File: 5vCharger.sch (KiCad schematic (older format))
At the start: 12 parts

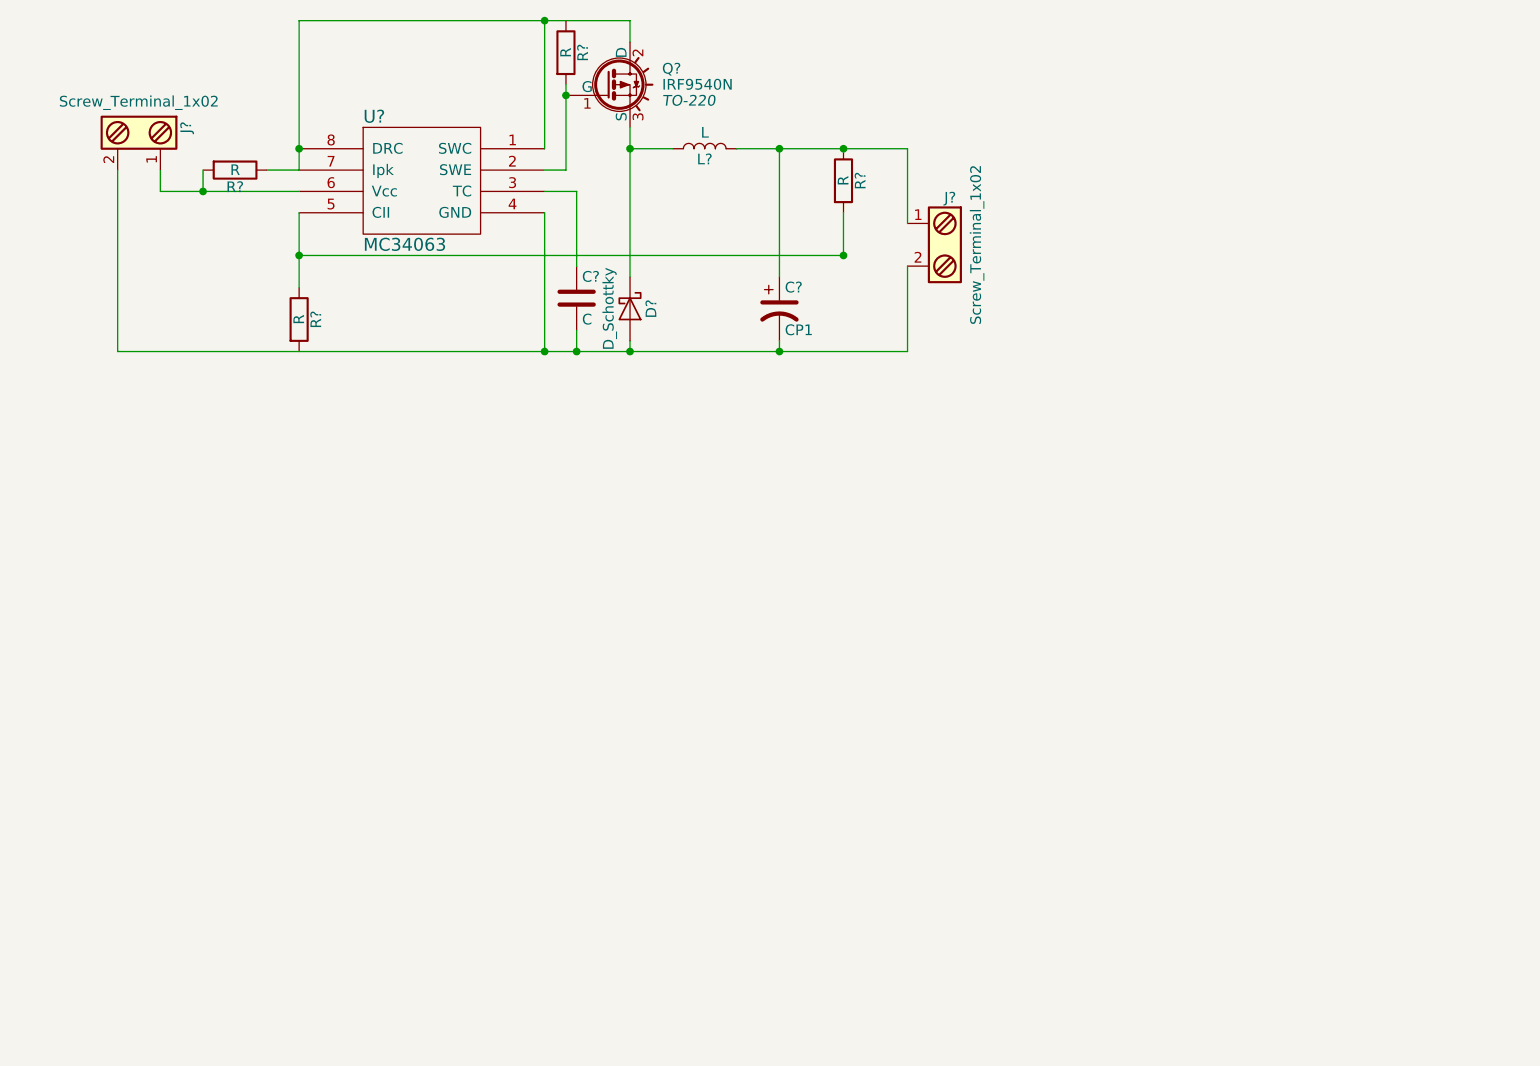
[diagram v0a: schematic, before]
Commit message: Set component values
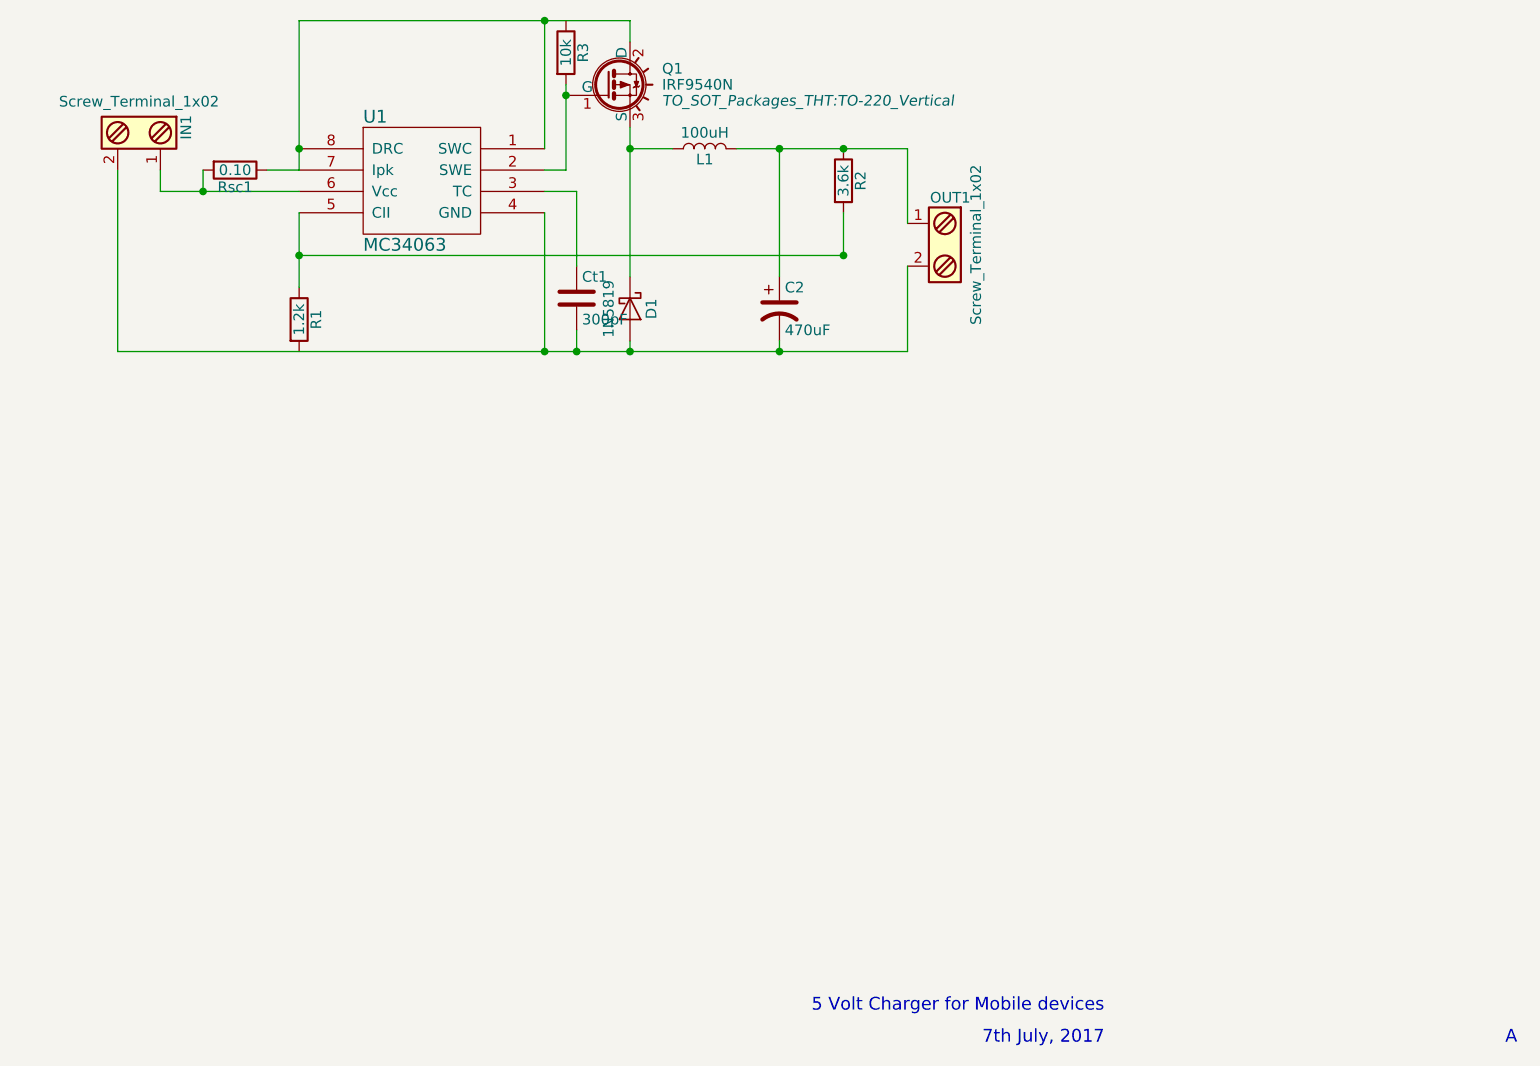
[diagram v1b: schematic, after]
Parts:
- C2: renamed from C?; value CP1 -> 470uF
- Ct1: renamed from C?; value C -> 300pF; footprint (none) -> Capacitors_THT:C_Disc_D4.3mm_W1.9mm_P5.00mm
- D1: renamed from D?; value D_Schottky -> 1N5819; footprint (none) -> Diodes_THT:D_DO-41_SOD81_P10.16mm_Horizontal
- IN1, OUT1: renamed from J?; footprint (none) -> Connectors_Terminal_Blocks:TerminalBlock_Pheonix_MKDS1.5-2pol
- L1: renamed from L?; value L -> 100uH
- Q1: renamed from Q?; footprint TO-220 -> TO_SOT_Packages_THT:TO-220_Vertical
- R1: renamed from R?; value R -> 1.2k
- R2: renamed from R?; value R -> 3.6k
- R3: renamed from R?; value R -> 10k
- Rsc1: renamed from R?; value R -> 0.10
- gave numbers to parts that had none: 1
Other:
- note added: "5 Volt Charger for Mobile devices"
- note added: "7th July, 2017"
- note added: "A"
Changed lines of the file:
@@
 LIBS:valves
 LIBS:MC34063
+LIBS:5vCharger-cache
 EELAYER 25 0
 EELAYER END
@@
 $EndDescr
 $Comp
-L MC34063 U?
+L MC34063 U1
 U 1 1 59883D9D
 P 5550 3650
-F 0 "U?" H 5250 4000 60  0000 L CNN
+F 0 "U1" H 5250 4000 60  0000 L CNN
 F 1 "MC34063" H 5250 3400 60  0000 L CNN
-F 2 "" H 5450 3650 60  0000 C CNN
+F 2 "" H 5450 3650 60  0001 C CNN
 F 3 "" H 5450 3650 60  0000 C CNN
 	1    5550 3650
@@
 Connection ~ 4950 3450
 $Comp
-L R R?
+L R Rsc1
 U 1 1 59883E1F
 P 4650 3550
-F 0 "R?" V 4730 3550 50  0000 C CNN
-F 1 "R" V 4650 3550 50  0000 C CNN
-F 2 "" V 4580 3550 50  0000 C CNN
+F 0 "Rsc1" V 4730 3550 50  0000 C CNN
+F 1 "0.10" V 4650 3550 50  0000 C CNN
+F 2 "" V 4580 3550 50  0001 C CNN
 F 3 "" H 4650 3550 50  0000 C CNN
 	1    4650 3550
@@
 Connection ~ 4500 3650
 $Comp
-L Screw_Terminal_1x02 J?
+L Screw_Terminal_1x02 IN1
 U 1 1 59883FF8
 P 4200 3350
-F 0 "J?" H 4200 3600 50  0000 C TNN
+F 0 "IN1" H 4200 3600 50  0000 C TNN
 F 1 "Screw_Terminal_1x02" V 4050 3350 50  0000 C TNN
-F 2 "" H 4200 3125 50  0001 C CNN
+F 2 "Connectors_Terminal_Blocks:TerminalBlock_Pheonix_MKDS1.5-2pol" H 4200 3125 50  0001 C CNN
 F 3 "" H 4175 3350 50  0001 C CNN
 	1    4200 3350
@@
 	4100 4400 7800 4400
 $Comp
-L IRF9540N Q?
+L IRF9540N Q1
 U 1 1 5988468A
 P 6400 3150
-F 0 "Q?" H 6650 3225 50  0000 L CNN
+F 0 "Q1" H 6650 3225 50  0000 L CNN
 F 1 "IRF9540N" H 6650 3150 50  0000 L CNN
-F 2 "TO-220" H 6650 3075 50  0000 L CIN
+F 2 "TO_SOT_Packages_THT:TO-220_Vertical" H 6650 3075 50  0000 L CIN
 F 3 "" H 6400 3150 50  0000 L CNN
 	1    6400 3150
@@
 $EndComp
 $Comp
-L R R?
+L R R3
 U 1 1 59884753
 P 6200 3000
-F 0 "R?" V 6280 3000 50  0000 C CNN
-F 1 "R" V 6200 3000 50  0000 C CNN
-F 2 "" V 6130 3000 50  0000 C CNN
+F 0 "R3" V 6280 3000 50  0000 C CNN
+F 1 "10k" V 6200 3000 50  0000 C CNN
+F 2 "" V 6130 3000 50  0001 C CNN
 F 3 "" H 6200 3000 50  0000 C CNN
 	1    6200 3000
@@
 	6500 2850 6500 2950
 $Comp
-L D_Schottky D?
+L D_Schottky D1
 U 1 1 598847EF
 P 6500 4200
-F 0 "D?" H 6500 4300 50  0000 C CNN
-F 1 "D_Schottky" H 6500 4100 50  0000 C CNN
-F 2 "" H 6500 4200 50  0000 C CNN
+F 0 "D1" H 6500 4300 50  0000 C CNN
+F 1 "1N5819" H 6500 4100 50  0000 C CNN
+F 2 "Diodes_THT:D_DO-41_SOD81_P10.16mm_Horizontal" H 6500 4200 50  0001 C CNN
 F 3 "" H 6500 4200 50  0000 C CNN
 	1    6500 4200
@@
 	6500 3350 6500 4050
 $Comp
-L L L?
+L L L1
 U 1 1 59884843
 P 6850 3450
-F 0 "L?" V 6800 3450 50  0000 C CNN
-F 1 "L" V 6925 3450 50  0000 C CNN
-F 2 "" H 6850 3450 50  0000 C CNN
+F 0 "L1" V 6800 3450 50  0000 C CNN
+F 1 "100uH" V 6925 3450 50  0000 C CNN
+F 2 "" H 6850 3450 50  0001 C CNN
 F 3 "" H 6850 3450 50  0000 C CNN
 	1    6850 3450
@@
 $EndComp
 $Comp
-L CP1 C?
+L CP1 C2
 U 1 1 59884893
 P 7200 4200
-F 0 "C?" H 7225 4300 50  0000 L CNN
-F 1 "CP1" H 7225 4100 50  0000 L CNN
-F 2 "" H 7200 4200 50  0000 C CNN
+F 0 "C2" H 7225 4300 50  0000 L CNN
+F 1 "470uF" H 7225 4100 50  0000 L CNN
+F 2 "" H 7200 4200 50  0001 C CNN
 F 3 "" H 7200 4200 50  0000 C CNN
 	1    7200 4200
@@
 Connection ~ 7200 3450
 $Comp
-L R R?
+L R R2
 U 1 1 5988498A
 P 7500 3600
-F 0 "R?" V 7580 3600 50  0000 C CNN
-F 1 "R" V 7500 3600 50  0000 C CNN
-F 2 "" V 7430 3600 50  0000 C CNN
+F 0 "R2" V 7580 3600 50  0000 C CNN
+F 1 "3.6k" V 7500 3600 50  0000 C CNN
+F 2 "" V 7430 3600 50  0001 C CNN
 F 3 "" H 7500 3600 50  0000 C CNN
 	1    7500 3600
@@
 Connection ~ 6200 3200
 $Comp
-L R R?
+L R R1
 U 1 1 59884CE2
 P 4950 4250
-F 0 "R?" V 5030 4250 50  0000 C CNN
-F 1 "R" V 4950 4250 50  0000 C CNN
-F 2 "" V 4880 4250 50  0000 C CNN
+F 0 "R1" V 5030 4250 50  0000 C CNN
+F 1 "1.2k" V 4950 4250 50  0000 C CNN
+F 2 "" V 4880 4250 50  0001 C CNN
 F 3 "" H 4950 4250 50  0000 C CNN
 	1    4950 4250
@@
 	7500 3950 7500 3750
 $Comp
-L C C?
+L C Ct1
 U 1 1 59884EE9
 P 6250 4150
-F 0 "C?" H 6275 4250 50  0000 L CNN
-F 1 "C" H 6275 4050 50  0000 L CNN
-F 2 "" H 6288 4000 50  0000 C CNN
+F 0 "Ct1" H 6275 4250 50  0000 L CNN
+F 1 "300pF" H 6275 4050 50  0000 L CNN
+F 2 "Capacitors_THT:C_Disc_D4.3mm_W1.9mm_P5.00mm" H 6288 4000 50  0001 C CNN
 F 3 "" H 6250 4150 50  0000 C CNN
 	1    6250 4150
@@
 Connection ~ 4950 3950
 $Comp
-L Screw_Terminal_1x02 J?
+L Screw_Terminal_1x02 OUT1
 U 1 1 59885326
 P 8000 3900
-F 0 "J?" H 8000 4150 50  0000 C TNN
+F 0 "OUT1" H 8000 4150 50  0000 C TNN
 F 1 "Screw_Terminal_1x02" V 7850 3900 50  0000 C TNN
-F 2 "" H 8000 3675 50  0001 C CNN
+F 2 "Connectors_Terminal_Blocks:TerminalBlock_Pheonix_MKDS1.5-2pol" H 8000 3675 50  0001 C CNN
 F 3 "" H 7975 3900 50  0001 C CNN
 	1    8000 3900
@@
 	6100 3450 6100 2850
 Connection ~ 6100 2850
+Text Notes 7350 7500 0    60   ~ 0
+5 Volt Charger for Mobile devices
+Text Notes 10600 7650 0    60   ~ 0
+A
+Text Notes 8150 7650 0    60   ~ 0
+7th July, 2017
 $EndSCHEMATC

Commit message: Generated netlist
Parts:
- C2: footprint (none) -> Capacitors_THT:CP_Radial_D14.0mm_P5.00mm
- L1: footprint (none) -> Choke_Toroid_ThroughHole:Choke_Toroid_5x10mm_Vertical
- R1, R2, R3: footprint (none) -> Resistors_THT:R_Axial_DIN0207_L6.3mm_D2.5mm_P10.16mm_Horizontal
- Rsc1: footprint (none) -> Resistors_THT:R_Axial_DIN0918_L18.0mm_D9.0mm_P7.62mm_Vertical
- U1: footprint (none) -> Housings_DIP:DIP-8_W7.62mm_LongPads
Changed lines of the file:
@@
 F 0 "U1" H 5250 4000 60  0000 L CNN
 F 1 "MC34063" H 5250 3400 60  0000 L CNN
-F 2 "" H 5450 3650 60  0001 C CNN
+F 2 "Housings_DIP:DIP-8_W7.62mm_LongPads" H 5450 3650 60  0001 C CNN
 F 3 "" H 5450 3650 60  0000 C CNN
 	1    5550 3650
@@
 F 0 "Rsc1" V 4730 3550 50  0000 C CNN
 F 1 "0.10" V 4650 3550 50  0000 C CNN
-F 2 "" V 4580 3550 50  0001 C CNN
+F 2 "Resistors_THT:R_Axial_DIN0918_L18.0mm_D9.0mm_P7.62mm_Vertical" V 4580 3550 50  0001 C CNN
 F 3 "" H 4650 3550 50  0000 C CNN
 	1    4650 3550
@@
 F 0 "R3" V 6280 3000 50  0000 C CNN
 F 1 "10k" V 6200 3000 50  0000 C CNN
-F 2 "" V 6130 3000 50  0001 C CNN
+F 2 "Resistors_THT:R_Axial_DIN0207_L6.3mm_D2.5mm_P10.16mm_Horizontal" V 6130 3000 50  0001 C CNN
 F 3 "" H 6200 3000 50  0000 C CNN
 	1    6200 3000
@@
 F 0 "L1" V 6800 3450 50  0000 C CNN
 F 1 "100uH" V 6925 3450 50  0000 C CNN
-F 2 "" H 6850 3450 50  0001 C CNN
+F 2 "Choke_Toroid_ThroughHole:Choke_Toroid_5x10mm_Vertical" H 6850 3450 50  0001 C CNN
 F 3 "" H 6850 3450 50  0000 C CNN
 	1    6850 3450
@@
 F 0 "C2" H 7225 4300 50  0000 L CNN
 F 1 "470uF" H 7225 4100 50  0000 L CNN
-F 2 "" H 7200 4200 50  0001 C CNN
+F 2 "Capacitors_THT:CP_Radial_D14.0mm_P5.00mm" H 7200 4200 50  0001 C CNN
 F 3 "" H 7200 4200 50  0000 C CNN
 	1    7200 4200
@@
 F 0 "R2" V 7580 3600 50  0000 C CNN
 F 1 "3.6k" V 7500 3600 50  0000 C CNN
-F 2 "" V 7430 3600 50  0001 C CNN
+F 2 "Resistors_THT:R_Axial_DIN0207_L6.3mm_D2.5mm_P10.16mm_Horizontal" V 7430 3600 50  0001 C CNN
 F 3 "" H 7500 3600 50  0000 C CNN
 	1    7500 3600
@@
 F 0 "R1" V 5030 4250 50  0000 C CNN
 F 1 "1.2k" V 4950 4250 50  0000 C CNN
-F 2 "" V 4880 4250 50  0001 C CNN
+F 2 "Resistors_THT:R_Axial_DIN0207_L6.3mm_D2.5mm_P10.16mm_Horizontal" V 4880 4250 50  0001 C CNN
 F 3 "" H 4950 4250 50  0000 C CNN
 	1    4950 4250

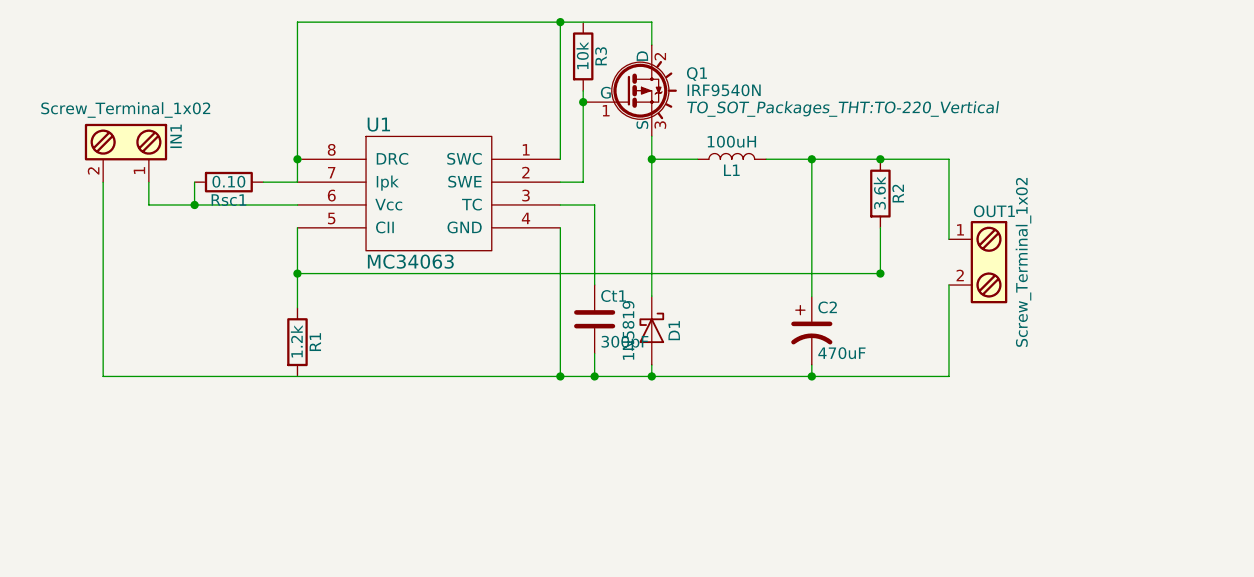
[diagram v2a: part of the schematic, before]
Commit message: Changed IC from MC34063 to an LM2596 rated at 3A
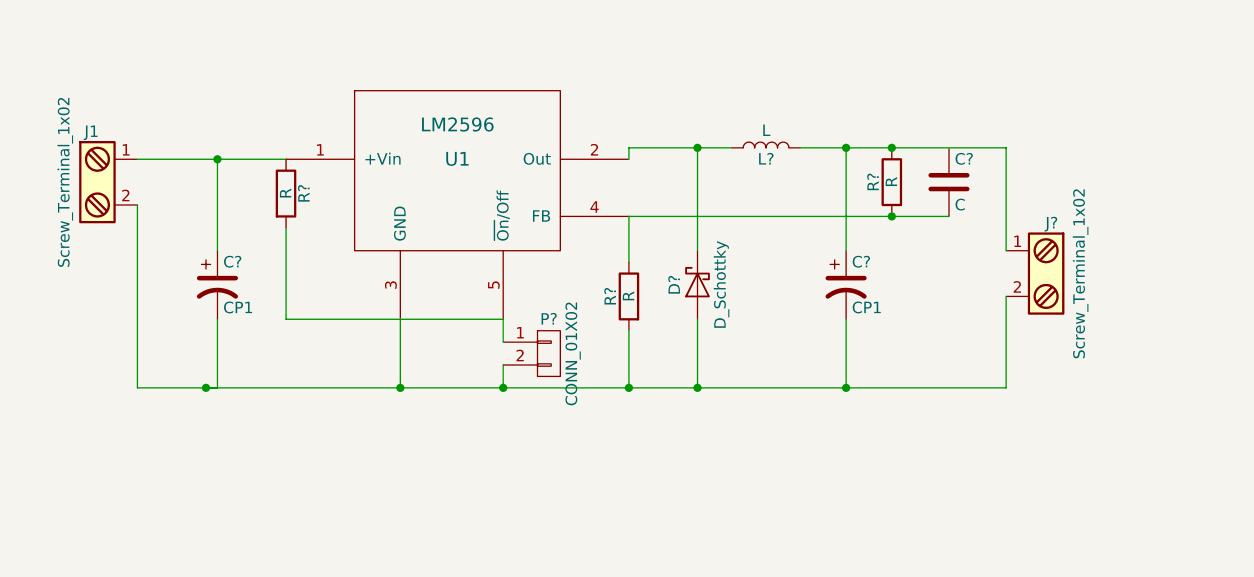
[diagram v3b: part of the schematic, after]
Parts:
- removed C2: 470uF, Capacitors_THT:CP_Radial_D14.0mm_P5.00mm, symbol CP1
- removed Ct1: 300pF, Capacitors_THT:C_Disc_D4.3mm_W1.9mm_P5.00mm, symbol C
- removed D1: 1N5819, Diodes_THT:D_DO-41_SOD81_P10.16mm_Horizontal, symbol D_Schottky
- removed IN1, OUT1: Screw_Terminal_1x02, Connectors_Terminal_Blocks:TerminalBlock_Pheonix_MKDS1.5-2pol, symbol Screw_Terminal_1x02
- removed L1: 100uH, Choke_Toroid_ThroughHole:Choke_Toroid_5x10mm_Vertical, symbol L
- removed Q1: IRF9540N, TO_SOT_Packages_THT:TO-220_Vertical, symbol IRF9540N
- removed R1: 1.2k, Resistors_THT:R_Axial_DIN0207_L6.3mm_D2.5mm_P10.16mm_Horizontal, symbol R
- removed R2: 3.6k, Resistors_THT:R_Axial_DIN0207_L6.3mm_D2.5mm_P10.16mm_Horizontal, symbol R
- removed R3: 10k, Resistors_THT:R_Axial_DIN0207_L6.3mm_D2.5mm_P10.16mm_Horizontal, symbol R
- removed Rsc1: 0.10, Resistors_THT:R_Axial_DIN0918_L18.0mm_D9.0mm_P7.62mm_Vertical, symbol R
- removed U1: MC34063, Housings_DIP:DIP-8_W7.62mm_LongPads, symbol MC34063
- added C? (x2): CP1, symbol CP1
- added C?: C, symbol C
- added D?: D_Schottky, symbol D_Schottky
- added J1, J?: Screw_Terminal_1x02, symbol Screw_Terminal_1x02
- added L?: L, symbol L
- added P?: CONN_01X02, symbol CONN_01X02
- added R? (x3): R, symbol R
- added U1: LM2596, symbol LM2596
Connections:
- new net: C?.1, J1.1, R?.1, U1.1 (+Vin)
- new net: D?.1 (K), L?.1, U1.2 (Out)
- new net: C?.2, C?.2, D?.2 (A), J1.2, J?.2, P?.2 (P2), R?.2, U1.3 (GND)
- new net: C?.2, R?.1, R?.2, U1.4 (FB)
- new net: P?.1 (P1), R?.2, U1.5 (~On~/Off)
- new net: C?.1, J?.1, L?.2, R?.1
